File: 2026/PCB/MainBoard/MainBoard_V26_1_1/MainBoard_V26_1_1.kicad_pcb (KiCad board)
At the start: 2 copper layers, 100 x 65 mm, 80 parts, among them J1 Raspberry_Pi_2_3, J15 TFT3, J16 CAN_CON, J2 fan, J4 metor, J6 Debug, J8 MOLEX MINISPOX, Q1 Q_NMOS_GSD, Q2 Q_NMOS_GSD, SW1 SW_MEC_5E, SW2 Ras_1, SW3 Ras_2, SW4 SW_Wuerth_450301014042, SW5 SW_MEC_5E, SW6 SW_MEC_5E, U1 STM32F446RETx, U10 MPU9250, U2 LMR51460FSQDRRRQ1, U3 MOUDLE-SEEEDUINO-XIAO, U5 MCP1703AT-3302E/CB, U6 BNO055, U8 MAX3051, Y1 CSTNE16M0V530000R0

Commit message: 配置一旦終わり。一部仮置き
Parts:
- removed J4: metor, Resistor_SMD:R_MiniMELF_MMA-0204
- removed J8: MOLEX MINISPOX, Connector_Molex:Molex_SPOX_5268-05A_1x05_P2.50mm_Horizontal
- added C14: 47u, Capacitor_SMD:C_0805_2012Metric_Pad1.18x1.45mm_HandSolder, B.Cu at (168.6, 105.8)
- added H2: MountingHole_Pad, MountingHole:MountingHole_3.2mm_M3_DIN965_Pad_TopBottom, F.Cu at (172.2, 116.5)
- added H2: MountingHole_Pad, MountingHole:MountingHole_3.2mm_M3_DIN965_Pad_TopBottom, F.Cu at (172.2, 67.5)
- added H2: MountingHole_Pad, MountingHole:MountingHole_3.2mm_M3_DIN965_Pad_TopBottom, F.Cu at (230.3, 67.5)
- added H2: MountingHole_Pad, MountingHole:MountingHole_3.2mm_M3_DIN965_Pad_TopBottom, F.Cu at (230.2, 116.5)
- added J3: MOLEX, Connector_Molex:Molex_SPOX_5268-04A_1x04_P2.50mm_Horizontal, F.Cu at (178.3, 117.3)
- added J5: Conn_01x05_Socket, Connector_JST:JST_PH_S5B-PH-K_1x05_P2.00mm_Horizontal, F.Cu at (198.3, 117.7)
- C10, C11, C13, C15, C16, C17, C18, C24, C9, J2, L1, LS1, Q1, Q2, R2, R20, R21, R3, R4, R7, U10, U2, U5, U6, U8: moved to B.Cu
- H1, H2, H4, H5: footprint MountingHole:MountingHole_3.2mm_M3_Pad_Via -> MountingHole:MountingHole_3.2mm_M3_DIN965_Pad_TopBottom
- moved U10 233.3 mm to (262.4, 93.8), turned to 180 degrees
- moved D14 225.5 mm to (258.6, 74.2)
- moved D13 225.4 mm to (258.6, 72.7)
- moved D15 225.3 mm to (258.6, 78.7), turned to 180 degrees
- moved D10 225.1 mm to (258.6, 71.2)
- moved D9 225.0 mm to (258.6, 69.7)
- moved D8 224.9 mm to (258.6, 68.2)
- moved D7 224.9 mm to (258.6, 66.7)
- moved D11 224.8 mm to (258.6, 77.2), turned to 180 degrees
- moved D3 224.5 mm to (258.6, 75.7), turned to 180 degrees
- moved R6 220.3 mm to (262.1, 75.7)
- moved R15 216.5 mm to (262.1, 71.2)
- moved R14 216.4 mm to (262.1, 69.7)
- moved R13 216.3 mm to (262.1, 68.2)
- moved R12 216.2 mm to (262.1, 66.7)
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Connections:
- LS1 pad P: VD -> +24V
- R10 pad 1: VD -> +24V
- R7 pad 1: VD -> +24V
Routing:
- net +3.3V: track 0.00 -> 23.4 mm
- net +5V: track 0.00 -> 7.32 mm
- net GND: track 0.00 -> 2.27 mm, vias 0 -> 2
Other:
- outline, holes or cut-outs redrawn

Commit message: 配線途中経過
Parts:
- moved LS1 32.7 mm to (187.8, 103.5)
- moved D6 27.1 mm to (192.1, 112.8), turned to 90 degrees
- moved C14 25.8 mm to (185.9, 86.7)
- moved R10 23.6 mm to (188.7, 112.1), turned to 90 degrees
- moved R11 22.3 mm to (190.2, 112.1), turned to -90 degrees
- moved R7 22.0 mm to (187.8, 110.8), turned to 0 degrees
- moved Q1 16.7 mm to (197.1, 100.3), turned to 180 degrees
- moved C15 14.3 mm to (170.3, 111.8), turned to -90 degrees
- moved R21 12.4 mm to (178.5, 108.4), turned to 90 degrees
- moved C17 11.9 mm to (179.4, 100.9), turned to 180 degrees
- moved ROTSW1 11.4 mm to (165.9, 72.1)
- moved SW2 11.3 mm to (192.5, 76.6)
- moved SW3 11.3 mm to (182.9, 76.7)
- moved R4 10.6 mm to (180.0, 108.4), turned to 90 degrees
- moved Q2 9.65 mm to (197.1, 106.1), turned to 180 degrees
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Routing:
- net +5V: track 7.32 -> 221.5 mm, vias 0 -> 1
- net +3.3V: track 23.4 -> 221.3 mm, vias 0 -> 3
- net I2C_SCL: track 0.00 -> 65.1 mm
- net R3: track 0.00 -> 53.9 mm
- net I2C_SDA: track 0.00 -> 52.7 mm
- net LED1: track 0.00 -> 47.3 mm, vias 0 -> 2
- net RAS_AUDIO: track 0.00 -> 47.1 mm, vias 0 -> 1
- net LED2: track 0.00 -> 45.6 mm, vias 0 -> 2
- net R2: track 0.00 -> 43.3 mm
- net Net-(C15-Pad2): track 0.00 -> 43.3 mm
- net HEART_BEAT_LED: track 0.00 -> 41.4 mm, vias 0 -> 2
- net T_CS: track 0.00 -> 40.8 mm
- net LED0: track 0.00 -> 35.2 mm, vias 0 -> 2
- net UART4_TX: track 0.00 -> 34.1 mm, vias 0 -> 2
- net R4: track 0.00 -> 33.6 mm
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
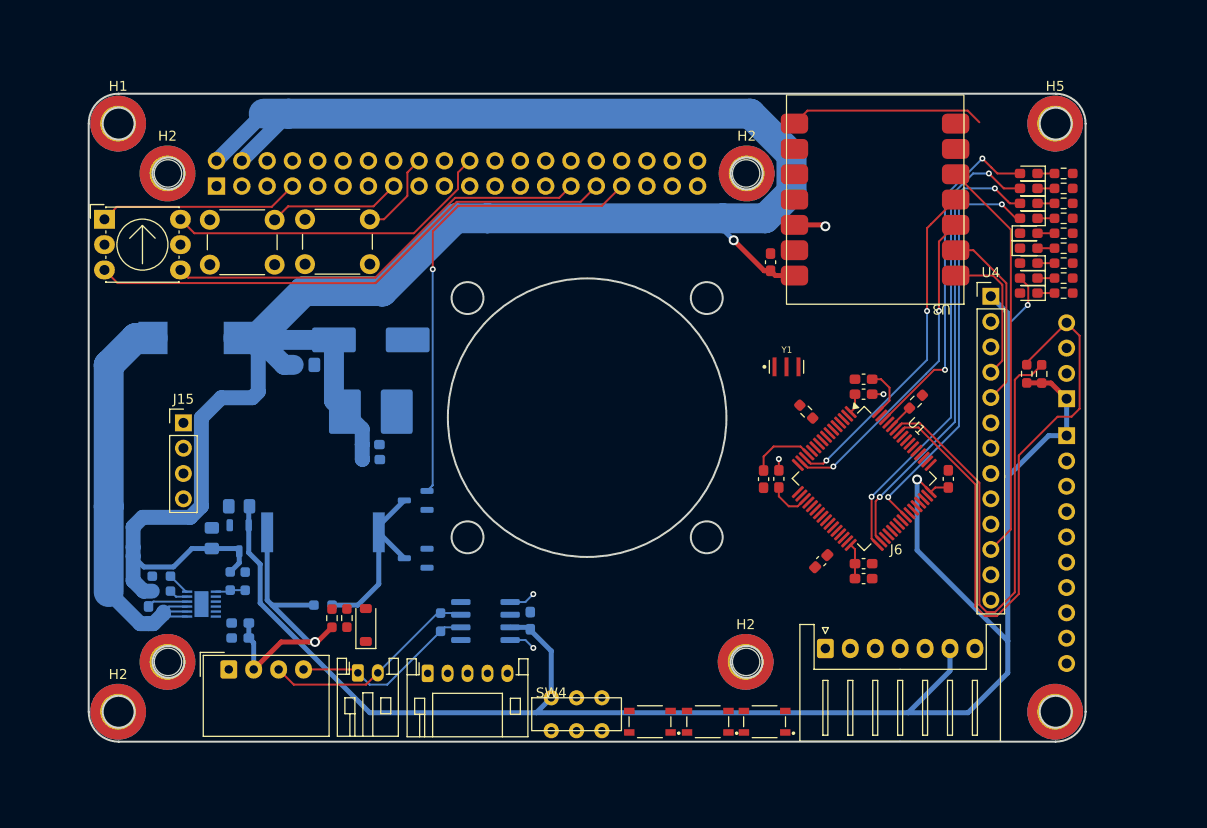
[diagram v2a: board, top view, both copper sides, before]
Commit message: メイン基板ひとまず完成
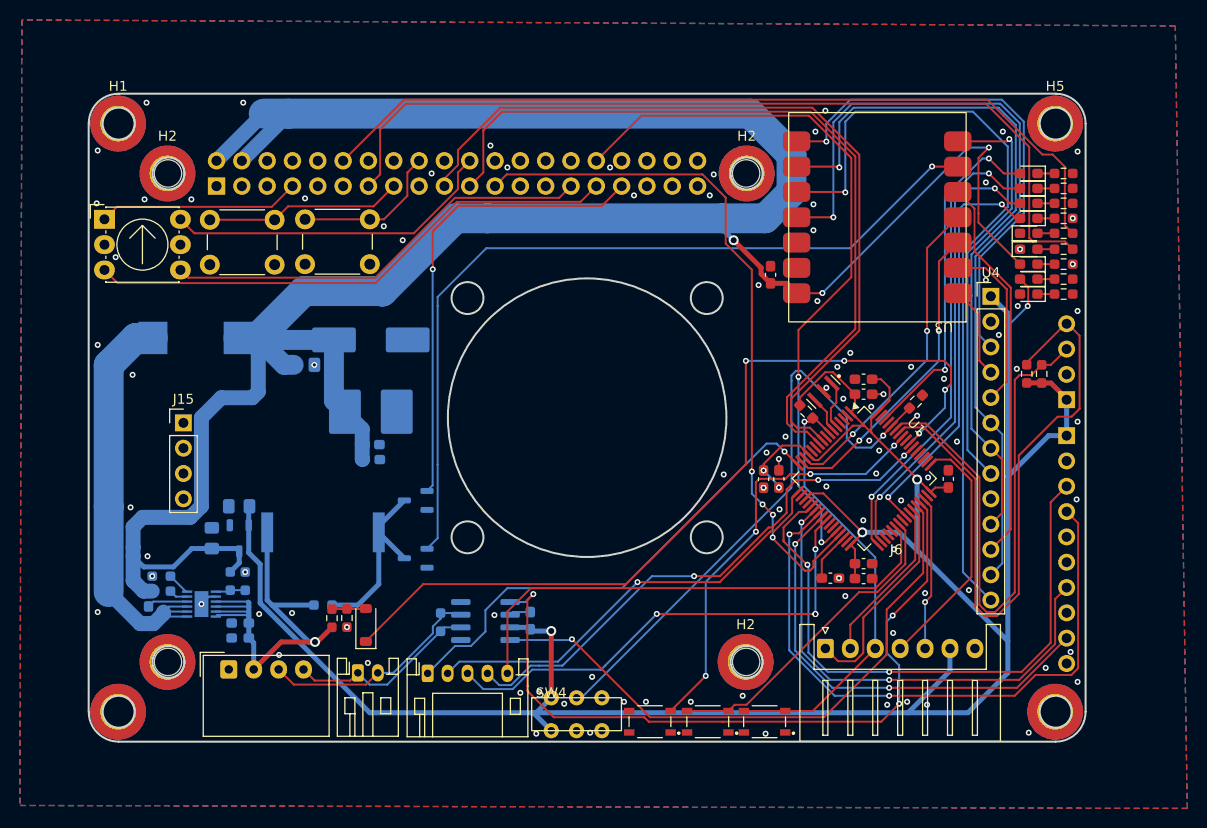
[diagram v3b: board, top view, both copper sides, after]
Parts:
- moved Y1 4.47 mm to (238.0, 89.4), turned to -135 degrees
- moved C1 1.94 mm to (238.7, 108.1), turned to 0 degrees
- moved U3 1.79 mm to (252.3, 61.4)
- moved C12 1.26 mm to (232.7, 77.7)
- moved U6 0.10 mm to (262.4, 90.2)
- moved D11 0.10 mm to (258.6, 78.1)
- moved D14 0.10 mm to (258.6, 75.1)
- moved D15 0.10 mm to (258.6, 79.6)
- moved D3 0.10 mm to (258.6, 76.6)
- moved R16 0.10 mm to (262.1, 78.1)
- moved R17 0.10 mm to (262.1, 79.6)
- moved R19 0.10 mm to (262.1, 75.1)
- moved R6 0.10 mm to (262.1, 76.6)
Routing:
- net LED_RAS2: track 0.00 -> 88.1 mm
- net BATTERY_MEASURE: track 0.00 -> 86.1 mm, vias 0 -> 4
- net LED_RAS1: track 0.00 -> 84.8 mm
- net UI_Audio: track 0.00 -> 83.3 mm, vias 0 -> 1
- net MOSI: track 0.00 -> 82.2 mm, vias 0 -> 1
- net SPI2.MOSI: track 0.00 -> 81.7 mm
- net SPI2.MISO: track 0.00 -> 79.8 mm
- net MISO: track 0.00 -> 78.7 mm, vias 0 -> 1
- net SPI2.CS: track 0.00 -> 72.9 mm, vias 0 -> 2
- net CAN1_TX: track 2.65 -> 74.6 mm, vias 1 -> 3
- net SCK: track 0.00 -> 71.6 mm, vias 0 -> 1
- net SPI2.CLK: track 0.00 -> 70.7 mm, vias 0 -> 4
- net SPI1.MOSI: track 0.00 -> 63.8 mm, vias 0 -> 2
- net SPI1.CLK: track 0.00 -> 60.0 mm, vias 0 -> 2
- net CAN1_RX: track 2.65 -> 60.5 mm
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- added copper zone on B.Cu, net GND
- added copper zone on F.Cu, net GND
